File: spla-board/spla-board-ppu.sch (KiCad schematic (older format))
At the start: 22 parts, among them J15 J_DPULL, J5 J_PPURESET, U10 SNES_PPU1, U11 SNES_PPU2, U12 VRAM, U13 VRAM

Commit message: pcb/schematic: Rework layout for 0.65mm PPU footprint, as well as other minor issues.
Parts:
- U10, U11: footprint SPLA:QFP-100_14x20mm_P0.635mm -> SPLA:QFP-100_14x20mm_P0.65mm
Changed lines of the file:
@@
 F 0 "U10" H 5650 9115 50  0000 C CNN
 F 1 "SNES_PPU1" H 5650 9024 50  0000 C CNN
-F 2 "SPLA:QFP-100_14x20mm_P0.635mm" H 5700 8300 50  0001 C CNN
+F 2 "SPLA:QFP-100_14x20mm_P0.65mm" H 5700 8300 50  0001 C CNN
 F 3 "" H 5700 8300 50  0001 C CNN
 F 4 "N/A" H 5650 6100 50  0001 C CNN "Digikey"
@@
 F 0 "U11" H 12200 9115 50  0000 C CNN
 F 1 "SNES_PPU2" H 12200 9024 50  0000 C CNN
-F 2 "SPLA:QFP-100_14x20mm_P0.635mm" H 12250 8300 50  0001 C CNN
+F 2 "SPLA:QFP-100_14x20mm_P0.65mm" H 12250 8300 50  0001 C CNN
 F 3 "" H 12250 8300 50  0001 C CNN
 F 4 "N/A" H 12200 6100 50  0001 C CNN "Digikey"

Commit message: schematic/pcb: Remove unnecessary 0-ohm resistors; renumber all parts by value.
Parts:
- renumbered BOM2 to BOM16, BOM3 to BOM17, C11 to C49, C8 to C5, C9 to C6, C10 to C7, C12 to C8, R24 to R30, R23 to R31, R22 to R32, R21 to R33, R20 to R34, R19 to R35, R18 to R36, R17 to R37, R11 to R5
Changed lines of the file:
@@
 ~5M
 $Comp
-L Device:R R11
+L Device:R R5
 U 1 1 5E6CC6A3
 P 10450 5800
-F 0 "R11" H 10520 5846 50  0000 L CNN
+F 0 "R5" H 10520 5846 50  0000 L CNN
 F 1 "100" H 10520 5755 50  0000 L CNN
 F 2 "Resistor_SMD:R_0603_1608Metric" V 10380 5800 50  0001 C CNN
@@
 $EndComp
 $Comp
-L Device:C C11
+L Device:C C49
 U 1 1 5E6CDC31
 P 10450 6100
-F 0 "C11" H 10568 6146 50  0000 L CNN
+F 0 "C49" H 10568 6146 50  0000 L CNN
 F 1 "56pF" H 10568 6055 50  0000 L CNN
 F 2 "Capacitor_SMD:C_0603_1608Metric" H 10488 5950 50  0001 C CNN
@@
 	11050 3850 11050 2450
 $Comp
-L Device:C_Small C8
+L Device:C_Small C5
 U 1 1 5E72F793
 P 6700 3100
-F 0 "C8" H 6792 3146 50  0000 L CNN
+F 0 "C5" H 6792 3146 50  0000 L CNN
 F 1 "0.1uF" H 6792 3055 50  0000 L CNN
 F 2 "Capacitor_SMD:C_0603_1608Metric" H 6700 3100 50  0001 C CNN
@@
 Connection ~ 6200 3000
 $Comp
-L Device:C_Small C12
+L Device:C_Small C8
 U 1 1 5E768AD3
 P 13000 3100
-F 0 "C12" H 13092 3146 50  0000 L CNN
+F 0 "C8" H 13092 3146 50  0000 L CNN
 F 1 "0.1uF" H 13092 3055 50  0000 L CNN
 F 2 "Capacitor_SMD:C_0603_1608Metric" H 13000 3100 50  0001 C CNN
@@
 Connection ~ 12850 3000
 $Comp
-L Device:C_Small C9
+L Device:C_Small C6
 U 1 1 5E7A4C4F
 P 9400 3200
-F 0 "C9" H 9492 3246 50  0000 L CNN
+F 0 "C6" H 9492 3246 50  0000 L CNN
 F 1 "0.1uF" H 9492 3155 50  0000 L CNN
 F 2 "Capacitor_SMD:C_0603_1608Metric" H 9400 3200 50  0001 C CNN
@@
 $EndComp
 $Comp
-L Device:C_Small C10
+L Device:C_Small C7
 U 1 1 5E88A2D5
 P 9400 5500
-F 0 "C10" H 9492 5546 50  0000 L CNN
+F 0 "C7" H 9492 5546 50  0000 L CNN
 F 1 "0.1uF" H 9492 5455 50  0000 L CNN
 F 2 "Capacitor_SMD:C_0603_1608Metric" H 9400 5500 50  0001 C CNN
@@
 ~HCLD
 $Comp
-L Device:R_Small R24
+L Device:R_Small R30
 U 1 1 5E6959A3
 P 3800 8750
-F 0 "R24" H 3859 8796 50  0000 L CNN
+F 0 "R30" H 3859 8796 50  0000 L CNN
 F 1 "10k" H 3859 8705 50  0000 L CNN
 F 2 "Resistor_SMD:R_0603_1608Metric" H 3800 8750 50  0001 C CNN
@@
 $EndComp
 $Comp
-L Device:R_Small R23
+L Device:R_Small R31
 U 1 1 5E814C80
 P 3550 8750
-F 0 "R23" H 3609 8796 50  0000 L CNN
+F 0 "R31" H 3609 8796 50  0000 L CNN
 F 1 "10k" H 3609 8705 50  0000 L CNN
 F 2 "Resistor_SMD:R_0603_1608Metric" H 3550 8750 50  0001 C CNN
@@
 $EndComp
 $Comp
-L Device:R_Small R22
+L Device:R_Small R32
 U 1 1 5E84A784
 P 3300 8750
-F 0 "R22" H 3359 8796 50  0000 L CNN
+F 0 "R32" H 3359 8796 50  0000 L CNN
 F 1 "10k" H 3359 8705 50  0000 L CNN
 F 2 "Resistor_SMD:R_0603_1608Metric" H 3300 8750 50  0001 C CNN
@@
 $EndComp
 $Comp
-L Device:R_Small R21
+L Device:R_Small R33
 U 1 1 5E84A78E
 P 3050 8750
-F 0 "R21" H 3109 8796 50  0000 L CNN
+F 0 "R33" H 3109 8796 50  0000 L CNN
 F 1 "10k" H 3109 8705 50  0000 L CNN
 F 2 "Resistor_SMD:R_0603_1608Metric" H 3050 8750 50  0001 C CNN
@@
 $EndComp
 $Comp
-L Device:R_Small R20
+L Device:R_Small R34
 U 1 1 5E880645
 P 2800 8750
-F 0 "R20" H 2859 8796 50  0000 L CNN
+F 0 "R34" H 2859 8796 50  0000 L CNN
 F 1 "10k" H 2859 8705 50  0000 L CNN
 F 2 "Resistor_SMD:R_0603_1608Metric" H 2800 8750 50  0001 C CNN
@@
 $EndComp
 $Comp
-L Device:R_Small R19
+L Device:R_Small R35
 U 1 1 5E88064F
 P 2550 8750
-F 0 "R19" H 2609 8796 50  0000 L CNN
+F 0 "R35" H 2609 8796 50  0000 L CNN
 F 1 "10k" H 2609 8705 50  0000 L CNN
 F 2 "Resistor_SMD:R_0603_1608Metric" H 2550 8750 50  0001 C CNN
@@
 $EndComp
 $Comp
-L Device:R_Small R18
+L Device:R_Small R36
 U 1 1 5E880659
 P 2300 8750
-F 0 "R18" H 2359 8796 50  0000 L CNN
+F 0 "R36" H 2359 8796 50  0000 L CNN
 F 1 "10k" H 2359 8705 50  0000 L CNN
 F 2 "Resistor_SMD:R_0603_1608Metric" H 2300 8750 50  0001 C CNN
@@
 $EndComp
 $Comp
-L Device:R_Small R17
+L Device:R_Small R37
 U 1 1 5E880663
 P 2050 8750
-F 0 "R17" H 2109 8796 50  0000 L CNN
+F 0 "R37" H 2109 8796 50  0000 L CNN
 F 1 "10k" H 2109 8705 50  0000 L CNN
 F 2 "Resistor_SMD:R_0603_1608Metric" H 2050 8750 50  0001 C CNN
@@
 	4650 2400 8050 2400
 $Comp
-L SPLA:BomExtra BOM3
+L SPLA:BomExtra BOM17
 U 1 1 5EAB9445
 P 8650 1550
-F 0 "BOM3" H 8780 1596 50  0000 L CNN
+F 0 "BOM17" H 8780 1596 50  0000 L CNN
 F 1 "Jumper" H 8780 1505 50  0000 L CNN
 F 2 "SPLA:BoM" H 8650 1550 50  0001 C CNN
@@
 $EndComp
 $Comp
-L SPLA:BomExtra BOM2
+L SPLA:BomExtra BOM16
 U 1 1 5EAB9764
 P 2550 9600
-F 0 "BOM2" H 2680 9646 50  0000 L CNN
+F 0 "BOM16" H 2680 9646 50  0000 L CNN
 F 1 "Jumper" H 2680 9555 50  0000 L CNN
 F 2 "SPLA:BoM" H 2550 9600 50  0001 C CNN

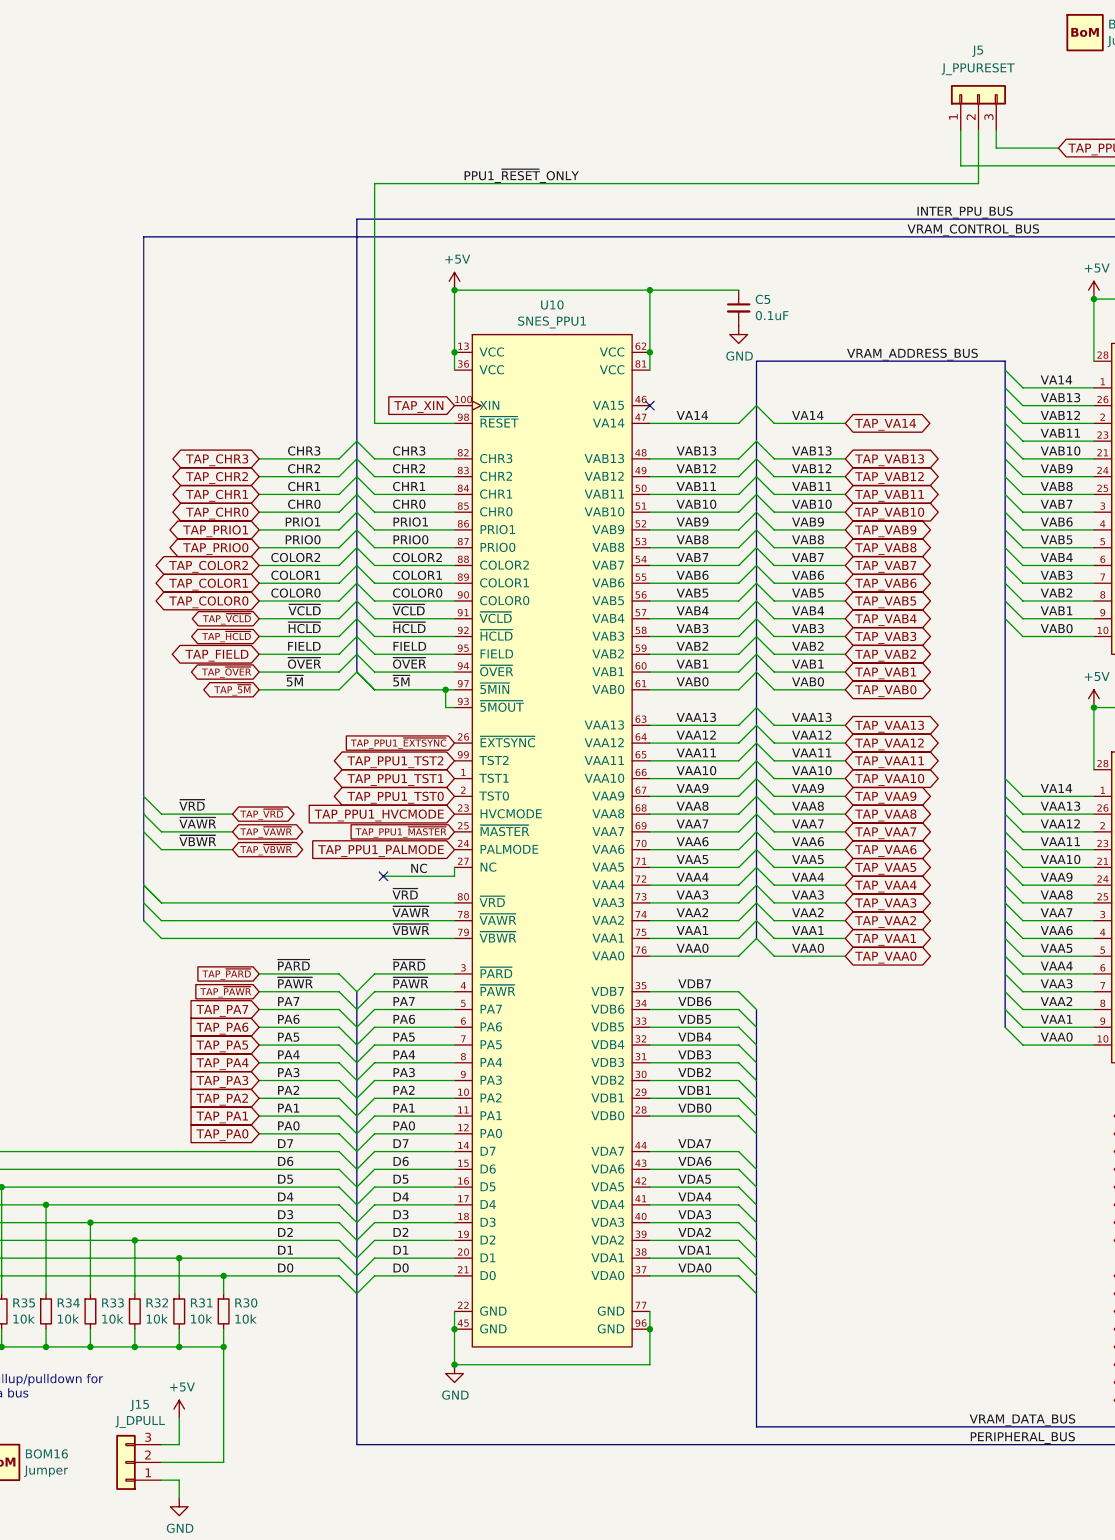
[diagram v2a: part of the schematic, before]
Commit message: schematic/pcb: Renumber connectors (J*).
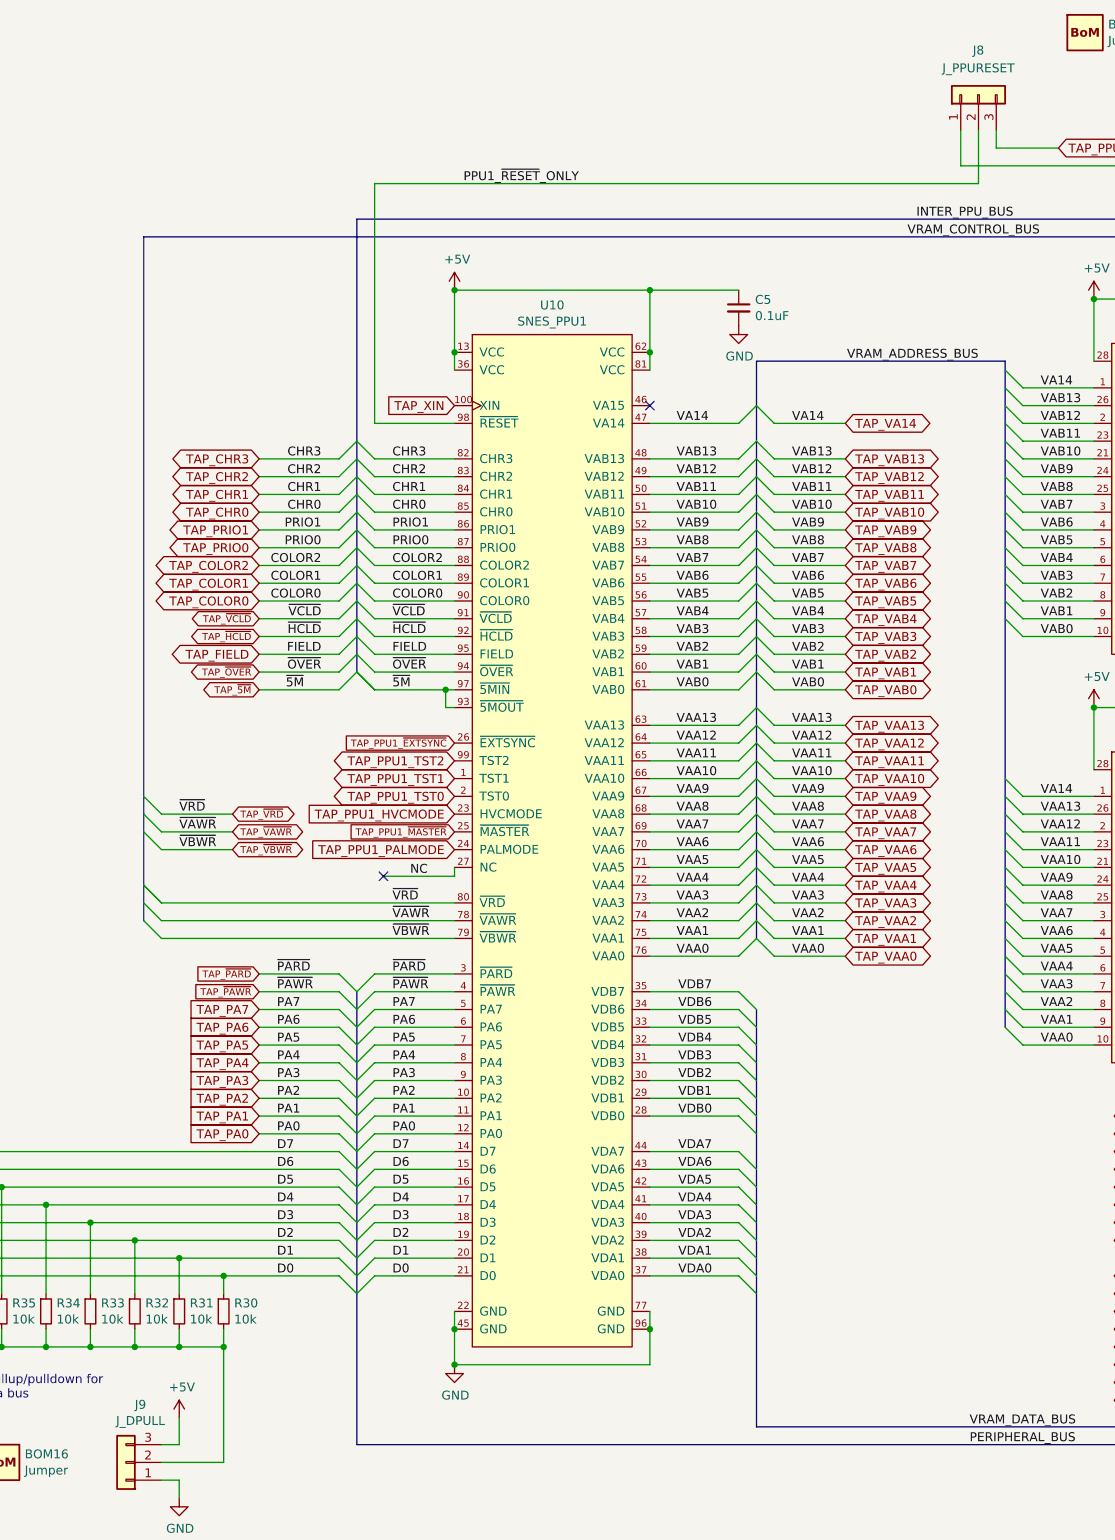
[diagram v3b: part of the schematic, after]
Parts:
- renumbered J5 to J8, J15 to J9
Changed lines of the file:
@@
 	2800 8950 3050 8950
 $Comp
-L Connector_Generic:Conn_01x03 J15
+L Connector_Generic:Conn_01x03 J9
 U 1 1 5EE846AD
 P 3250 9600
-F 0 "J15" H 3168 9275 50  0000 C CNN
+F 0 "J9" H 3168 9275 50  0000 C CNN
 F 1 "J_DPULL" H 3168 9366 50  0000 C CNN
 F 2 "Connector_PinHeader_2.54mm:PinHeader_1x03_P2.54mm_Vertical" H 3250 9600 50  0001 C CNN
@@
 TAP_PPU1_~RESET~
 $Comp
-L Connector_Generic:Conn_01x03 J5
+L Connector_Generic:Conn_01x03 J8
 U 1 1 5E72EA03
 P 8050 1900
-F 0 "J5" V 8300 1900 50  0000 C CNN
+F 0 "J8" V 8300 1900 50  0000 C CNN
 F 1 "J_PPURESET" V 8200 1900 50  0000 C CNN
 F 2 "Connector_PinHeader_2.54mm:PinHeader_1x03_P2.54mm_Vertical" H 8050 1900 50  0001 C CNN

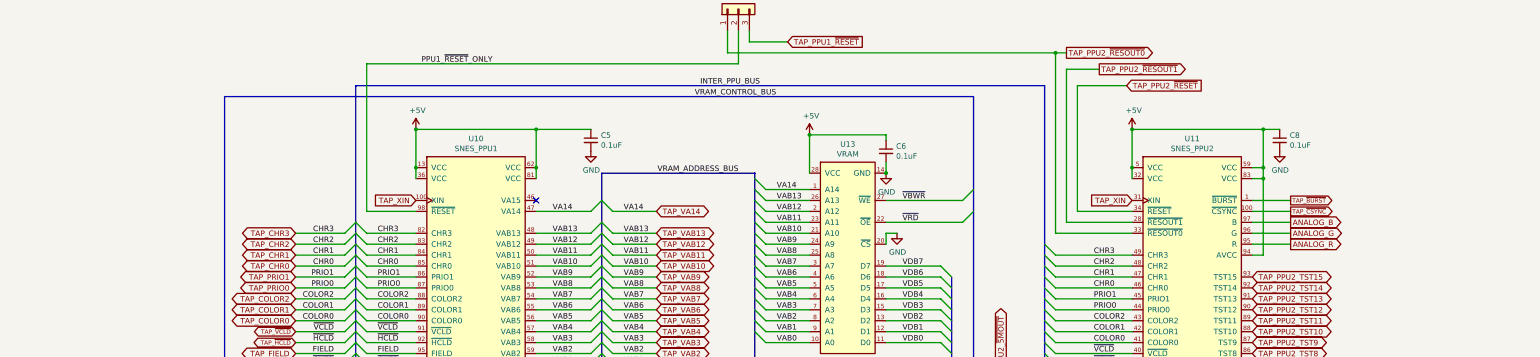
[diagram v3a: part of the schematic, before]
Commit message: schematic/pcb: Seperate PPU2 AVCC; add more PPU decoupling.
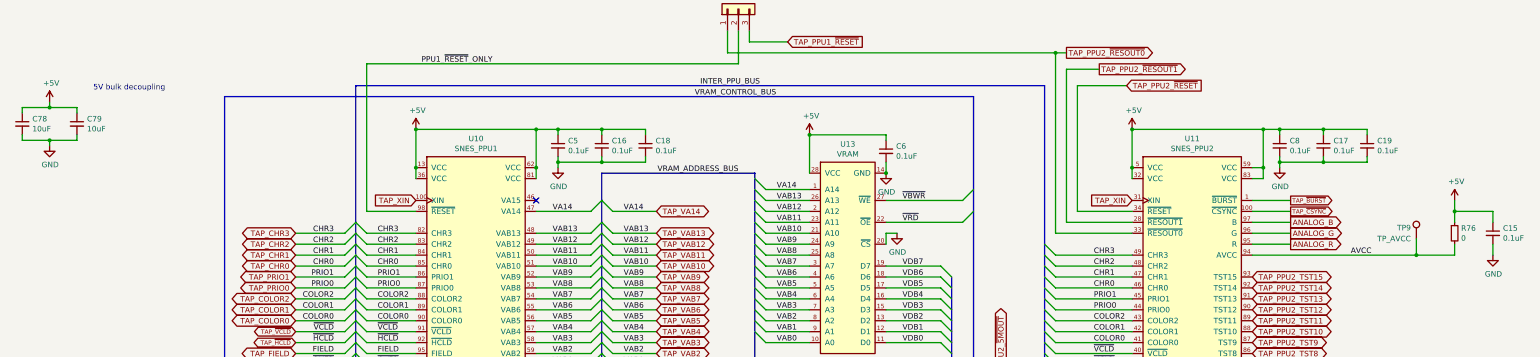
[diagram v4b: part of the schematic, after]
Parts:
- added C15, C16, C17, C18, C19: 0.1uF, Capacitor_SMD:C_0603_1608Metric, symbol Device:C_Small
- added C78, C79: 10uF, Capacitor_SMD:C_0805_2012Metric, symbol Device:C_Small
- added R76: 0, Resistor_SMD:R_0603_1608Metric, symbol Device:R_Small
- added TP9: TP_AVCC, TestPoint:TestPoint_Pad_D1.0mm, symbol Connector:TestPoint
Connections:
- net +5V: now also C15.1, C16.1, C17.1, C18.1, C19.1, C78.1, C79.1, R76.1; no longer U11.94 (AVCC)
- net GND: now also C15.2, C16.2, C17.2, C18.2, C19.2, C78.2, C79.2
- new net AVCC: R76.2, TP9.1, U11.94 (AVCC)
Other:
- note added: "5V bulk decoupling"
- moved on the sheet: C5, C8

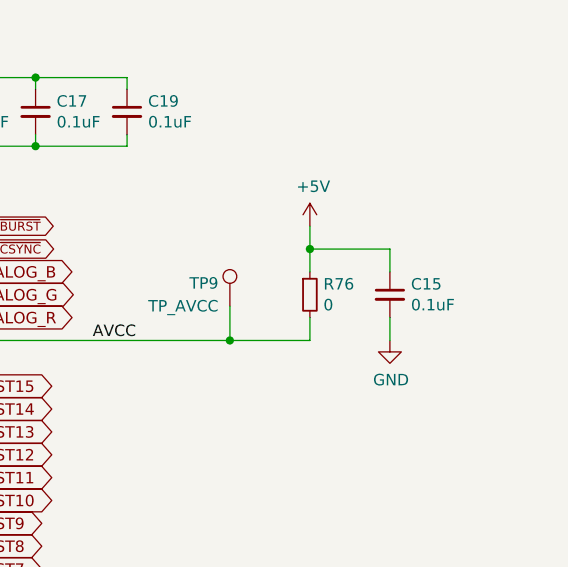
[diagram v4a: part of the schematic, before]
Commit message: schematic: Fix AVCC power flag.
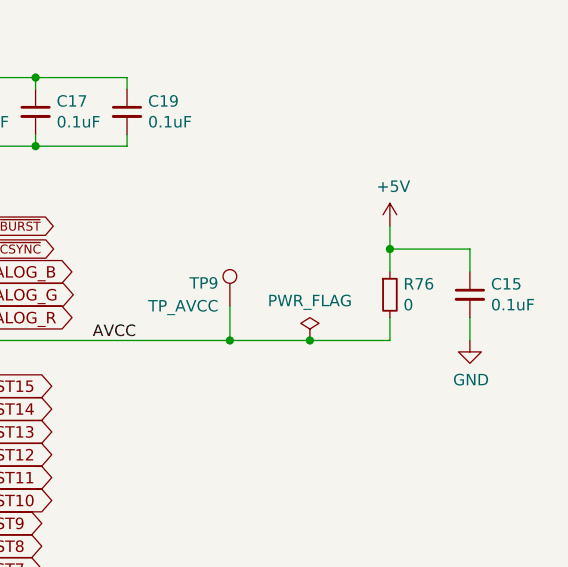
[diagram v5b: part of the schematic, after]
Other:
- moved on the sheet: C15, R76
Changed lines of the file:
@@
 L Device:R_Small R76
 U 1 1 5F65D68F
-P 14600 3950
-F 0 "R76" H 14659 3996 50  0000 L CNN
-F 1 "0" H 14659 3905 50  0000 L CNN
-F 2 "Resistor_SMD:R_0603_1608Metric" H 14600 3950 50  0001 C CNN
-F 3 "~" H 14600 3950 50  0001 C CNN
-F 4 "2019-RK73Z1JTTDCT-ND" H 14600 3950 50  0001 C CNN "Digikey"
-F 5 "KOA Speer Electronics Inc." H 14600 3950 50  0001 C CNN "Manufacturer"
-F 6 "RK73Z1JTTD" H 14600 3950 50  0001 C CNN "Manufacturer Id"
-	1    14600 3950
+P 14950 3950
+F 0 "R76" H 15009 3996 50  0000 L CNN
+F 1 "0" H 15009 3905 50  0000 L CNN
+F 2 "Resistor_SMD:R_0603_1608Metric" H 14950 3950 50  0001 C CNN
+F 3 "~" H 14950 3950 50  0001 C CNN
+F 4 "2019-RK73Z1JTTDCT-ND" H 14950 3950 50  0001 C CNN "Digikey"
+F 5 "KOA Speer Electronics Inc." H 14950 3950 50  0001 C CNN "Manufacturer"
+F 6 "RK73Z1JTTD" H 14950 3950 50  0001 C CNN "Manufacturer Id"
+	1    14950 3950
 	1    0    0    -1
 $EndComp
@@
 L power:+5V #PWR0247
 U 1 1 5F660676
-P 14600 3650
-F 0 "#PWR0247" H 14600 3500 50  0001 C CNN
-F 1 "+5V" H 14615 3823 50  0000 C CNN
-F 2 "" H 14600 3650 50  0001 C CNN
-F 3 "" H 14600 3650 50  0001 C CNN
-	1    14600 3650
-	1    0    0    -1
-$EndComp
-Wire Wire Line
-	14600 4150 14600 4050
+P 14950 3650
+F 0 "#PWR0247" H 14950 3500 50  0001 C CNN
+F 1 "+5V" H 14965 3823 50  0000 C CNN
+F 2 "" H 14950 3650 50  0001 C CNN
+F 3 "" H 14950 3650 50  0001 C CNN
+	1    14950 3650
+	1    0    0    -1
+$EndComp
+Wire Wire Line
+	14950 4150 14950 4050
 Text Label 13650 4150 0    50   ~ 0
 AVCC
 Wire Wire Line
-	14600 3750 14600 3850
+	14950 3750 14950 3850
 $Comp
 L Device:C_Small C15
 U 1 1 5F716A75
-P 14950 3950
-F 0 "C15" H 15042 3996 50  0000 L CNN
-F 1 "0.1uF" H 15042 3905 50  0000 L CNN
-F 2 "Capacitor_SMD:C_0603_1608Metric" H 14950 3950 50  0001 C CNN
-F 3 "~" H 14950 3950 50  0001 C CNN
-F 4 "490-16477-1-ND" H 14950 3950 50  0001 C CNN "Digikey"
-F 5 "Murata Electronics" H 14950 3950 50  0001 C CNN "Manufacturer"
-F 6 "GCJ188R71E104KA12D" H 14950 3950 50  0001 C CNN "Manufacturer Id"
-	1    14950 3950
-	1    0    0    -1
-$EndComp
-Wire Wire Line
-	14600 3750 14950 3750
-Wire Wire Line
-	14950 3750 14950 3850
-Connection ~ 14600 3750
-Wire Wire Line
-	14950 4050 14950 4150
+P 15300 3950
+F 0 "C15" H 15392 3996 50  0000 L CNN
+F 1 "0.1uF" H 15392 3905 50  0000 L CNN
+F 2 "Capacitor_SMD:C_0603_1608Metric" H 15300 3950 50  0001 C CNN
+F 3 "~" H 15300 3950 50  0001 C CNN
+F 4 "490-16477-1-ND" H 15300 3950 50  0001 C CNN "Digikey"
+F 5 "Murata Electronics" H 15300 3950 50  0001 C CNN "Manufacturer"
+F 6 "GCJ188R71E104KA12D" H 15300 3950 50  0001 C CNN "Manufacturer Id"
+	1    15300 3950
+	1    0    0    -1
+$EndComp
+Wire Wire Line
+	14950 3750 15300 3750
+Wire Wire Line
+	15300 3750 15300 3850
+Connection ~ 14950 3750
+Wire Wire Line
+	15300 4050 15300 4150
 $Comp
 L power:GND #PWR0249
 U 1 1 5F7FACC2
-P 14950 4150
-F 0 "#PWR0249" H 14950 3900 50  0001 C CNN
-F 1 "GND" H 14955 3977 50  0000 C CNN
-F 2 "" H 14950 4150 50  0001 C CNN
-F 3 "" H 14950 4150 50  0001 C CNN
-	1    14950 4150
-	1    0    0    -1
-$EndComp
-Wire Wire Line
-	14600 3650 14600 3750
+P 15300 4150
+F 0 "#PWR0249" H 15300 3900 50  0001 C CNN
+F 1 "GND" H 15305 3977 50  0000 C CNN
+F 2 "" H 15300 4150 50  0001 C CNN
+F 3 "" H 15300 4150 50  0001 C CNN
+	1    15300 4150
+	1    0    0    -1
+$EndComp
+Wire Wire Line
+	14950 3650 14950 3750
 Wire Wire Line
 	6800 3000 6800 3050
@@
 Wire Wire Line
 	14250 4000 14250 4150
+Wire Wire Line
+	12750 4150 14250 4150
+Wire Wire Line
+	14250 4150 14600 4150
 Connection ~ 14250 4150
-Wire Wire Line
-	14250 4150 14600 4150
-Wire Wire Line
-	12750 4150 14250 4150
+$Comp
+L power:PWR_FLAG #FLG?
+U 1 1 603660AC
+P 14600 4150
+F 0 "#FLG?" H 14600 4225 50  0001 C CNN
+F 1 "PWR_FLAG" H 14600 4323 50  0000 C CNN
+F 2 "" H 14600 4150 50  0001 C CNN
+F 3 "~" H 14600 4150 50  0001 C CNN
+	1    14600 4150
+	1    0    0    -1
+$EndComp
+Connection ~ 14600 4150
+Wire Wire Line
+	14600 4150 14950 4150
 Wire Bus Line
 	10200 2700 10200 6050
